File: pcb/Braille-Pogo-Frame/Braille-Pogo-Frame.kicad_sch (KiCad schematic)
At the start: 5 parts, among them J10 Screw_Terminal_01x02, J9 Conn_01x02

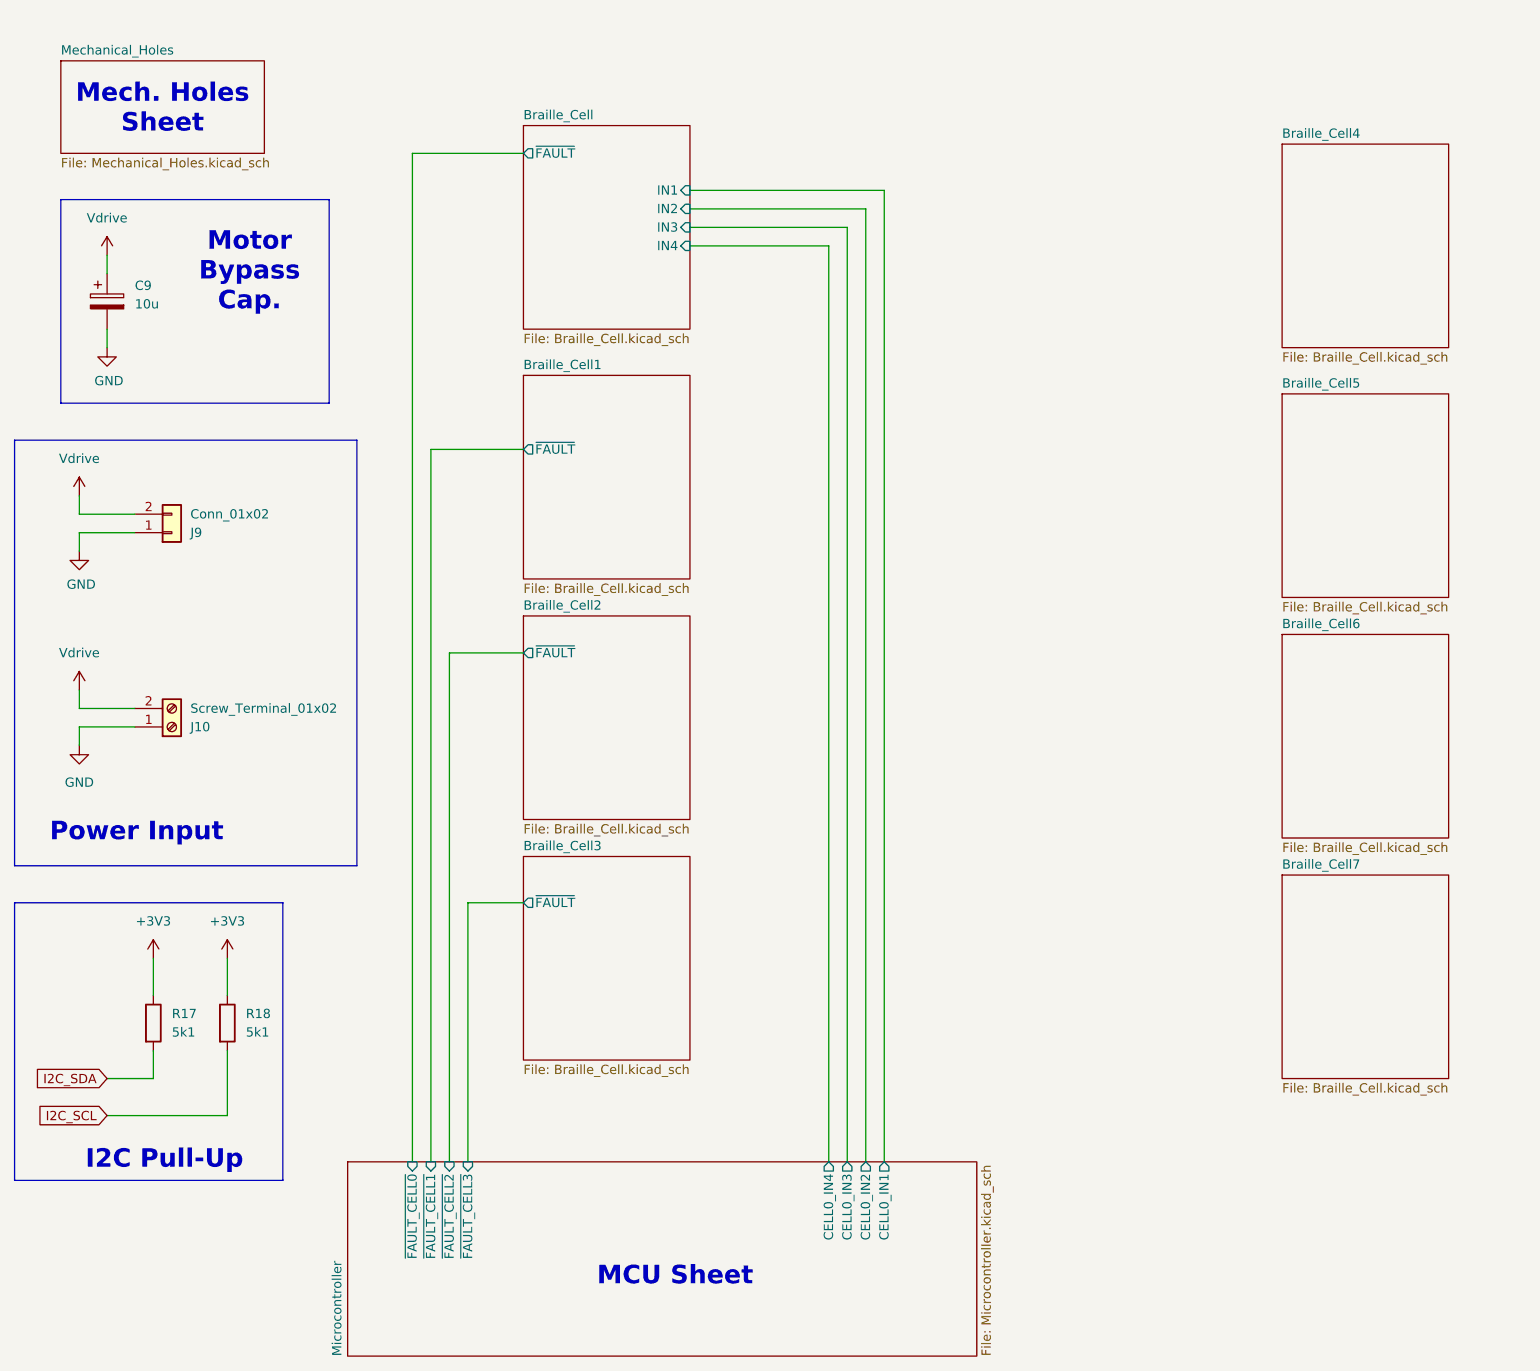
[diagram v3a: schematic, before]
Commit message: PCB: Place motor drivers and horiz. rail mounts
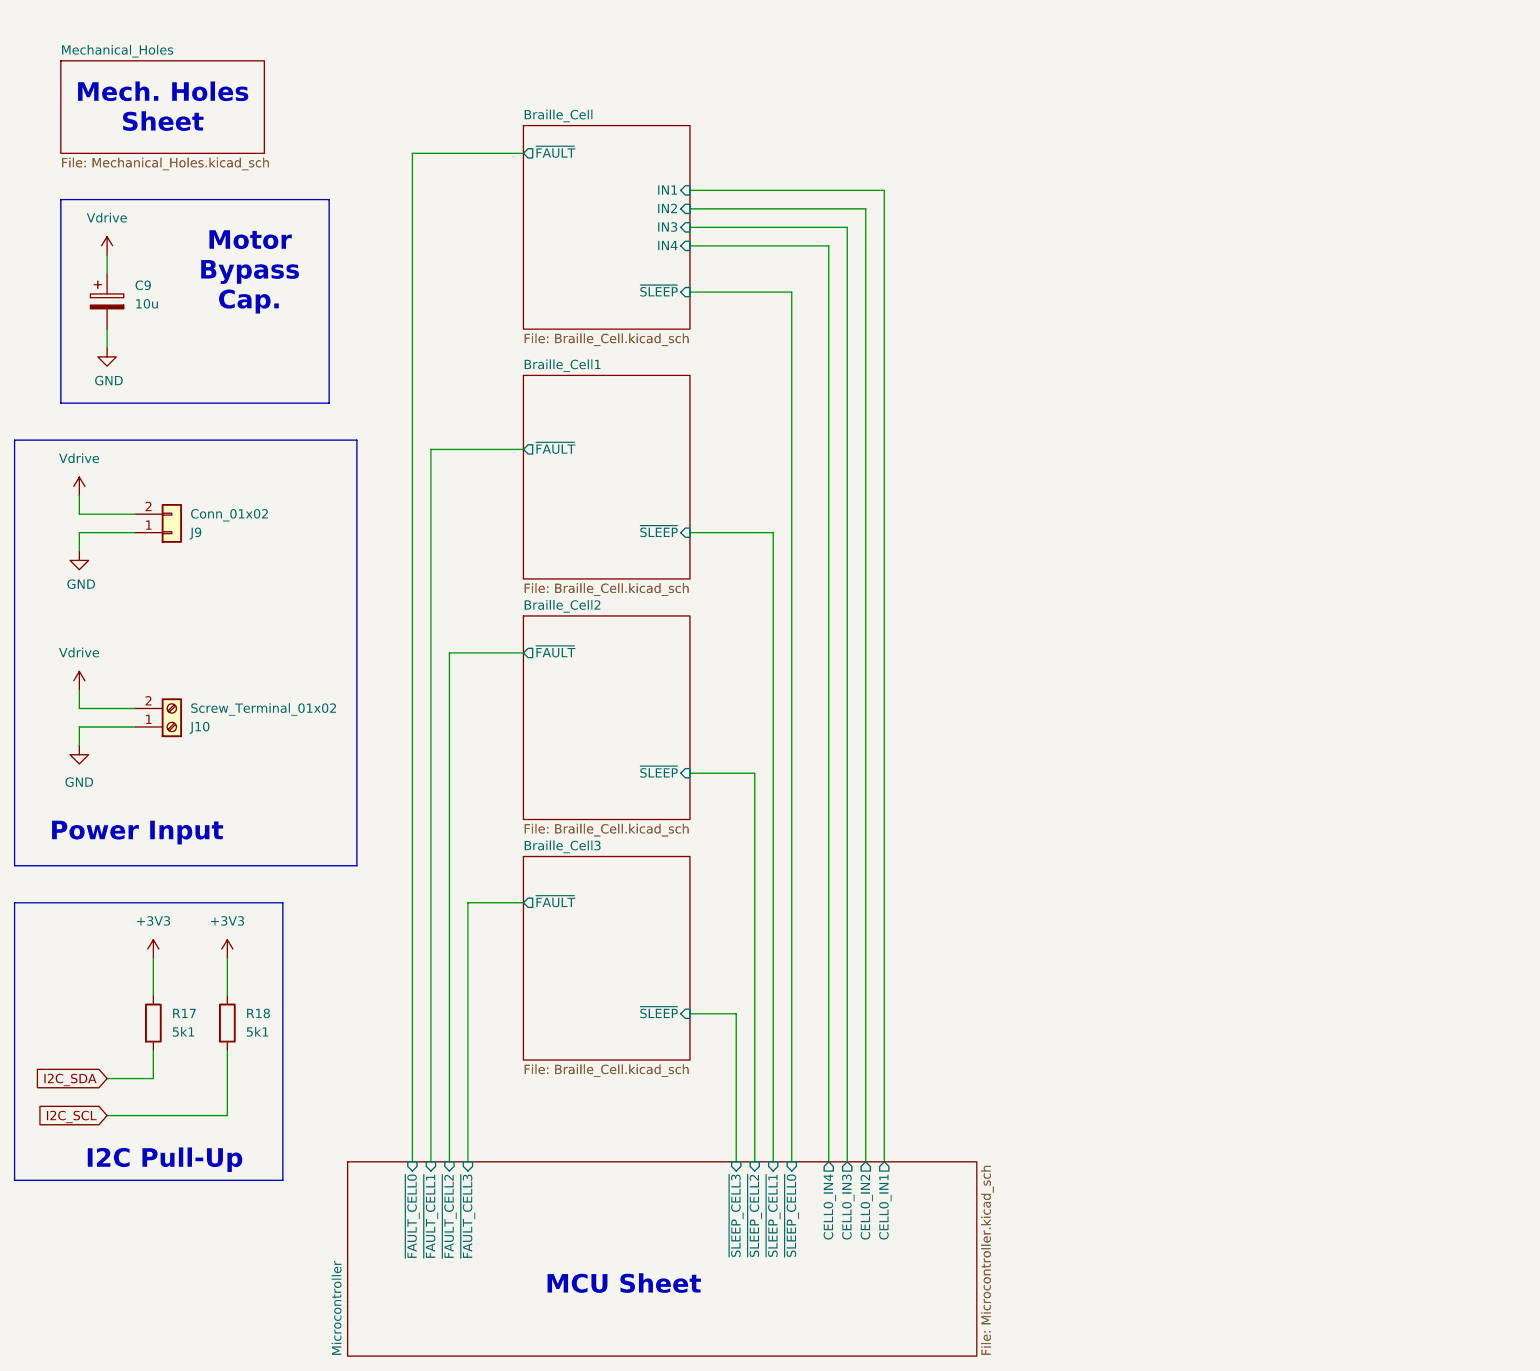
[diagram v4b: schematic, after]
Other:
- removed sheet Braille_Cell4
- removed sheet Braille_Cell5
- removed sheet Braille_Cell6
- removed sheet Braille_Cell7
- sheet Braille_Cell ports: added ~{SLEEP}; removed none
- sheet Braille_Cell1 ports: added ~{SLEEP}; removed none
- sheet Braille_Cell2 ports: added ~{SLEEP}; removed none
- sheet Braille_Cell3 ports: added ~{SLEEP}; removed none
- sheet Microcontroller ports: added ~{SLEEP_CELL0}, ~{SLEEP_CELL1}, ~{SLEEP_CELL2}, ~{SLEEP_CELL3}; removed none
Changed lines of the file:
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@@
+	(wire
+		(pts
+			(xy 119.38 152.4) (xy 113.03 152.4)
+		)
+		(stroke
+			(width 0)
+			(type default)
+		)
+	)
+	(wire
+		(pts
+			(xy 113.03 86.36) (xy 124.46 86.36)
+		)
+		(stroke
+			(width 0)
+			(type default)
+		)
+	)
 	(wire
 		(pts
@@
 	(wire
 		(pts
+			(xy 124.46 86.36) (xy 124.46 172.72)
+		)
+		(stroke
+			(width 0)
+			(type default)
+		)
+	)
+	(wire
+		(pts
 			(xy 33.02 166.37) (xy 49.53 166.37)
 		)
@@
 	(wire
 		(pts
+			(xy 119.38 172.72) (xy 119.38 152.4)
+		)
+		(stroke
+			(width 0)
+			(type default)
+		)
+	)
+	(wire
+		(pts
 			(xy 132.08 172.72) (xy 132.08 46.99)
 		)
@@
 	(wire
 		(pts
+			(xy 127 53.34) (xy 127 172.72)
+		)
+		(stroke
+			(width 0)
+			(type default)
+		)
+	)
+	(wire
+		(pts
 			(xy 77.47 172.72) (xy 77.47 74.93)
 		)
@@
 	(wire
 		(pts
+			(xy 121.92 172.72) (xy 121.92 119.38)
+		)
+		(stroke
+			(width 0)
+			(type default)
+		)
+	)
+	(wire
+		(pts
 			(xy 29.21 110.49) (xy 29.21 107.95)
 		)
@@
 	(wire
 		(pts
+			(xy 121.92 119.38) (xy 113.03 119.38)
+		)
+		(stroke
+			(width 0)
+			(type default)
+		)
+	)
+	(wire
+		(pts
 			(xy 113.03 39.37) (xy 139.7 39.37)
 		)
@@
 		(pts
 			(xy 139.7 39.37) (xy 139.7 172.72)
+		)
+		(stroke
+			(width 0)
+			(type default)
+		)
+	)
+	(wire
+		(pts
+			(xy 127 53.34) (xy 113.03 53.34)
 		)
 		(stroke
@@
 	(text "MCU Sheet"
 		(exclude_from_sim no)
-		(at 110.998 188.468 0)
+		(at 103.886 189.738 0)
 		(effects
 			(font
@@
 			)
 		)
+		(pin "~{SLEEP}" input
+			(at 113.03 152.4 0)
+			(effects
+				(font
+					(size 1.27 1.27)
+				)
+				(justify right)
+			)
+		)
 		(instances
 			(project "Braille-Pogo-Frame"
@@
 	)
 	(sheet
-		(at 194.31 33.02)
-		(size 22.86 27.94)
-		(fields_autoplaced yes)
-		(stroke
-			(width 0.1524)
-			(type solid)
-		)
-		(fill
-			(color 0 0 0 0.0000)
-		)
-		(property "Sheetname" "Braille_Cell4"
-			(at 194.31 32.3084 0)
-			(effects
-				(font
-					(size 1.27 1.27)
-				)
-				(justify left bottom)
-			)
-		)
-		(property "Sheetfile" "Braille_Cell.kicad_sch"
-			(at 194.31 61.5446 0)
-			(effects
-				(font
-					(size 1.27 1.27)
-				)
-				(justify left top)
-			)
-		)
-		(instances
-			(project "Braille-Pogo-Frame"
-				(path "/f7fdfeea-4cd4-4338-ad68-f9089a17ed6f"
-					(page "7")
-				)
-			)
-		)
-	)
-	(sheet
-		(at 194.31 133.35)
-		(size 22.86 27.94)
-		(fields_autoplaced yes)
-		(stroke
-			(width 0.1524)
-			(type solid)
-		)
-		(fill
-			(color 0 0 0 0.0000)
-		)
-		(property "Sheetname" "Braille_Cell7"
-			(at 194.31 132.6384 0)
-			(effects
-				(font
-					(size 1.27 1.27)
-				)
-				(justify left bottom)
-			)
-		)
-		(property "Sheetfile" "Braille_Cell.kicad_sch"
-			(at 194.31 161.8746 0)
-			(effects
-				(font
-					(size 1.27 1.27)
-				)
-				(justify left top)
-			)
-		)
-		(instances
-			(project "Braille-Pogo-Frame"
-				(path "/f7fdfeea-4cd4-4338-ad68-f9089a17ed6f"
-					(page "10")
-				)
-			)
-		)
-	)
-	(sheet
 		(at 90.17 97.79)
 		(size 22.86 27.94)
@@
 				)
 				(justify left)
+			)
+		)
+		(pin "~{SLEEP}" input
+			(at 113.03 119.38 0)
+			(effects
+				(font
+					(size 1.27 1.27)
+				)
+				(justify right)
 			)
 		)
@@
 	)
 	(sheet
-		(at 194.31 100.33)
-		(size 22.86 27.94)
-		(fields_autoplaced yes)
-		(stroke
-			(width 0.1524)
-			(type solid)
-		)
-		(fill
-			(color 0 0 0 0.0000)
-		)
-		(property "Sheetname" "Braille_Cell6"
-			(at 194.31 99.6184 0)
-			(effects
-				(font
-					(size 1.27 1.27)
-				)
-				(justify left bottom)
-			)
-		)
-		(property "Sheetfile" "Braille_Cell.kicad_sch"
-			(at 194.31 128.8546 0)
-			(effects
-				(font
-					(size 1.27 1.27)
-				)
-				(justify left top)
-			)
-		)
-		(instances
-			(project "Braille-Pogo-Frame"
-				(path "/f7fdfeea-4cd4-4338-ad68-f9089a17ed6f"
-					(page "9")
-				)
-			)
-		)
-	)
-	(sheet
 		(at 90.17 30.48)
 		(size 22.86 27.94)
@@
 		(pin "IN1" input
 			(at 113.03 39.37 0)
+			(effects
+				(font
+					(size 1.27 1.27)
+				)
+				(justify right)
+			)
+		)
+		(pin "~{SLEEP}" input
+			(at 113.03 53.34 0)
 			(effects
 				(font
@@
 	)
 	(sheet
-		(at 194.31 67.31)
-		(size 22.86 27.94)
-		(fields_autoplaced yes)
-		(stroke
-			(width 0.1524)
-			(type solid)
-		)
-		(fill
-			(color 0 0 0 0.0000)
-		)
-		(property "Sheetname" "Braille_Cell5"
-			(at 194.31 66.5984 0)
-			(effects
-				(font
-					(size 1.27 1.27)
-				)
-				(justify left bottom)
-			)
-		)
-		(property "Sheetfile" "Braille_Cell.kicad_sch"
-			(at 194.31 95.8346 0)
-			(effects
-				(font
-					(size 1.27 1.27)
-				)
-				(justify left top)
-			)
-		)
-		(instances
-			(project "Braille-Pogo-Frame"
-				(path "/f7fdfeea-4cd4-4338-ad68-f9089a17ed6f"
-					(page "8")
-				)
-			)
-		)
-	)
-	(sheet
 		(at 66.04 172.72)
 		(size 86.36 26.67)
@@
 		(pin "CELL0_IN4" output
 			(at 132.08 172.72 90)
+			(effects
+				(font
+					(size 1.27 1.27)
+				)
+				(justify right)
+			)
+		)
+		(pin "~{SLEEP_CELL1}" input
+			(at 124.46 172.72 90)
+			(effects
+				(font
+					(size 1.27 1.27)
+				)
+				(justify right)
+			)
+		)
+		(pin "~{SLEEP_CELL2}" input
+			(at 121.92 172.72 90)
+			(effects
+				(font
+					(size 1.27 1.27)
+				)
+				(justify right)
+			)
+		)
+		(pin "~{SLEEP_CELL0}" input
+			(at 127 172.72 90)
+			(effects
+				(font
+					(size 1.27 1.27)
+				)
+				(justify right)
+			)
+		)
+		(pin "~{SLEEP_CELL3}" input
+			(at 119.38 172.72 90)
 			(effects
 				(font
@@
 			)
 		)
+		(pin "~{SLEEP}" input
+			(at 113.03 86.36 0)
+			(effects
+				(font
+					(size 1.27 1.27)
+				)
+				(justify right)
+			)
+		)
